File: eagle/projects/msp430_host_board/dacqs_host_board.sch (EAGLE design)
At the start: 68 parts, among them J1 MOL-KK-4P-V, J10 MOL-KK-3P-V, J11 CLM-112-02-L-D, J13 MOL-KK-2-V, J2 MOL-KK-4P-V, J3 MOL-KK-4P-V, J4 MOL-KK-4P-V, J5 MOL-KK-5P-V, J6 MOL-KK-3P-V, J7 MOL-KK-5P-V, J8 MOL-KK-3P-RA, J9 MOL-KK-3P-V, U1 Value, U2 Value, U3 PCT2075D,118, U4 MS560702BA03-50, U5 TPS61240DRVR, U6 LP5907_DBV_5, Y1 32.768kHz, Y2 4MHz, Y3 32.768kHz, Y4 4MHz

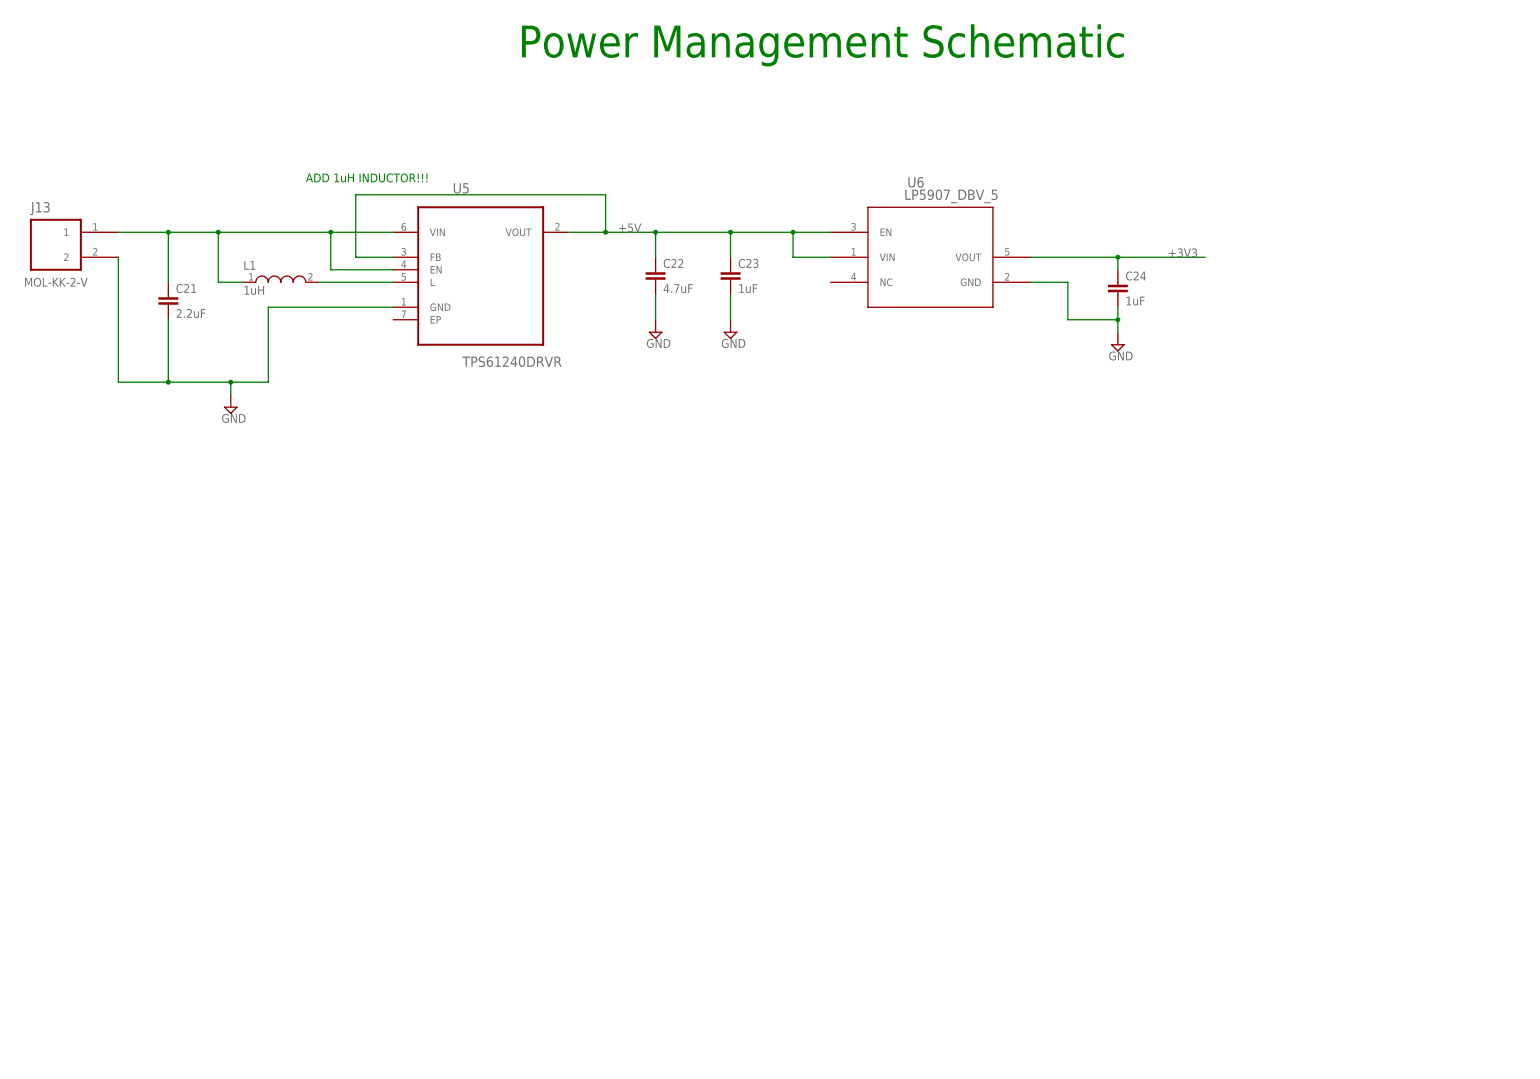
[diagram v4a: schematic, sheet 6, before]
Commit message: Added charging, current sense and motor battery voltage sensing
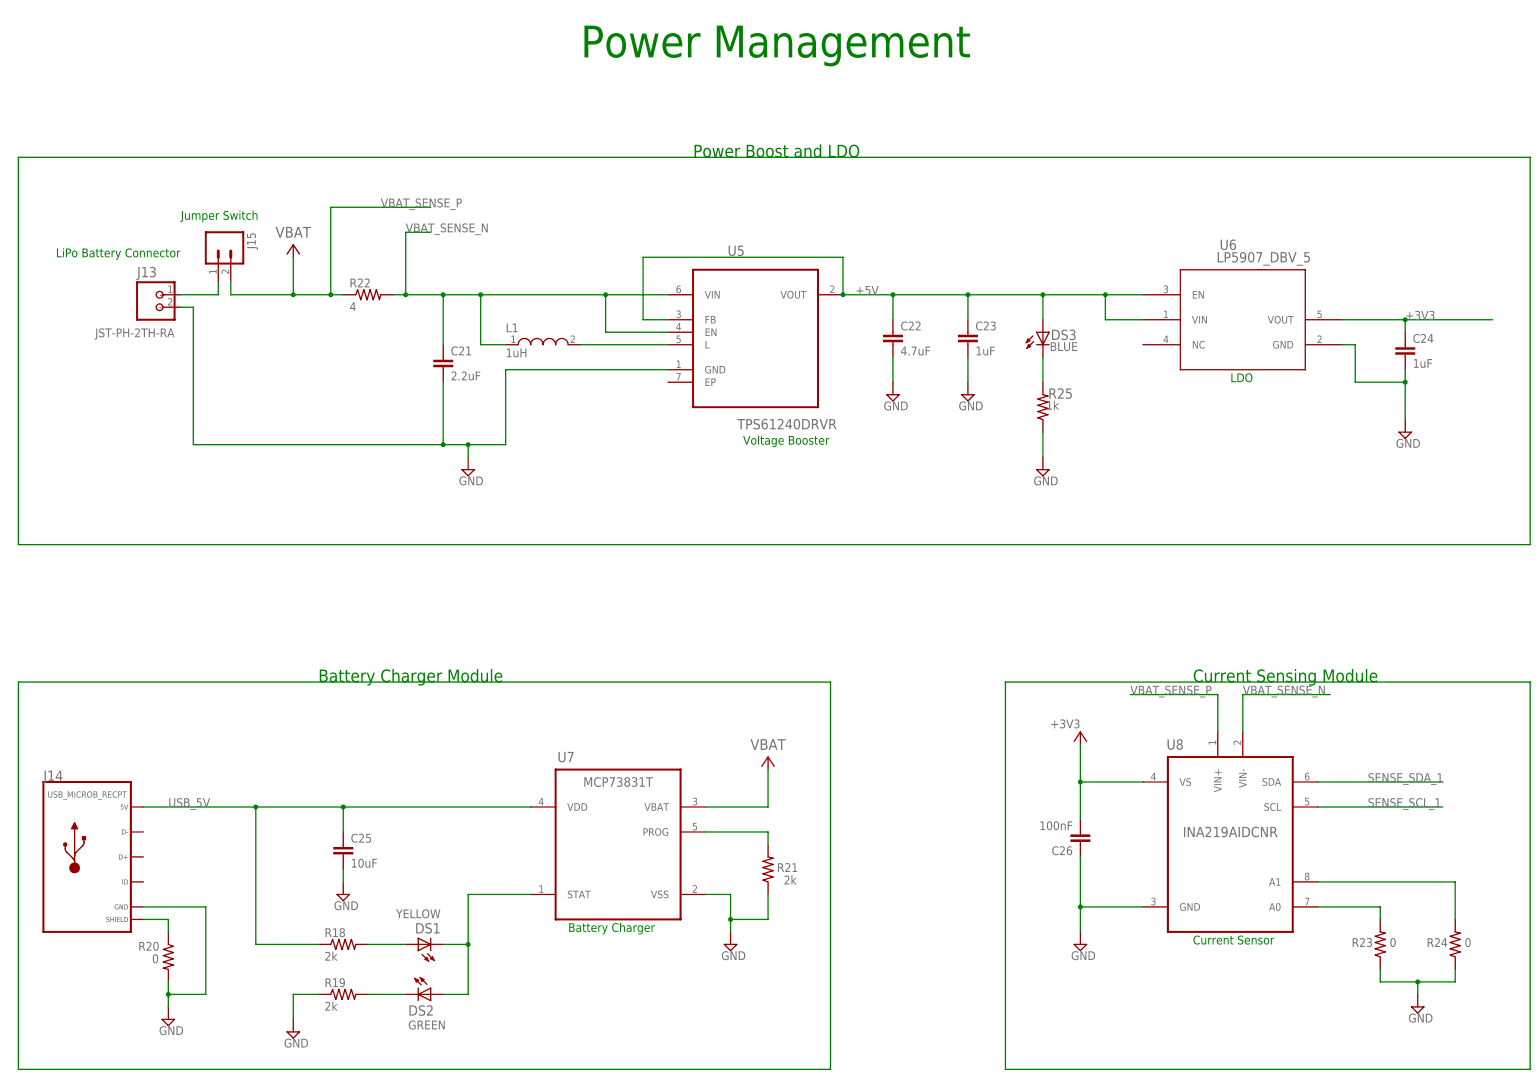
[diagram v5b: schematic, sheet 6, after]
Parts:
- added BAT1: (no value), daqcs_host:BC9VPC
- added C25: 10uF, daqcs_host:CAP_10UF0_0603
- added C26: 100nF, daqcs_host:CAP_100NF0_0603
- added DS1: YELLOW, daqcs_host:LED_Y2V0WURTH_0603
- added DS2: GREEN, daqcs_host:LED_G3V2WURTH_0603
- added DS3: BLUE, daqcs_host:LED_B3V2WURTH_0603
- added J14: USB_MICROB_RECPT, daqcs_host:USB_B_MICRO_RIGHT
- added J15: (no value), daqcs_host:M02PTH
- added J16: MOL-KK-2-RA, daqcs_host:MOLKK_2PIN_2RA_2RA
- added J18: MOL-KK-2-V, daqcs_host:MOLKK_2PIN2V_2V
- added R18, R19, R21: 2k, daqcs_host:RES_2R0_0603
- added R20, R23, R24: 0, daqcs_host:RES_0R0_0603
- added R22: 4, daqcs_host:RES_4R0_0603
- added R25: 1k, daqcs:RES_1R0_0603
- added R28: 10k, daqcs_host:RES_10R0_0603
- added R29: 27k, daqcs_host:RES_27R0_0603
- added U7: MCP73831T, daqcs_host:MCP73831T-2ATI/OT
- added U8: INA219AIDCNR, daqcs_host:INA219AIDCNR
- added U9: STD12NF06LT4, daqcs_host:STD12NF06LT4
- J13: value MOL-KK-2-V -> JST-PH-2TH-RA; device daqcs_host:MOLKK_2PIN2V_2V -> daqcs_host:JST-PH-2TH-RA_2TH-RA
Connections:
- new net 4V2_BAT: J18.1, R28.1
- new net CUTDOWN_EN: U1.P4.0_A8, U9.1
- new net MOTOR_BAT_VSENSE_1: R28.2, R29.2, U1.P3.0_A12_C12
- new net N$38: J14.SLD, R20.1
- new net N$39: J16.1
- new net N$40: BAT1.V+, J16.2
- new net N$41: DS2.C, R19.2
- new net N$42: DS1.C, DS2.A, U7.STAT
- new net N$43: DS1.A, R18.2
- new net N$44: R21.2, U7.PROG
- new net N$45: R23.2, U8.A0
- new net N$46: R24.2, U8.A1
- new net N$47: DS3.C, R25.2
- new net USB_5V: C25.1, J14.5V, R18.1, U7.VDD
- new net VBAT: U7.VBAT
- new net VBAT_SENSE_N: C21.1, L1.1, R22.2, U5.EN, U5.VIN, U8.VIN-
- new net VBAT_SENSE_P: J15.2, R22.1, U8.VIN+
- net +3V3: now also C26.2, U8.VS
- net +5V: now also DS3.A
- net GND: now also C25.2, C26.1, J14.GND, J18.2, R19.1, R20.2, R21.1, R23.1, R24.1, R25.1, R29.1, U7.VSS, U8.GND
- net N$36: now also J15.1; no longer C21.1, L1.1, U5.EN, U5.VIN
- net SENSE_SCL_1: now also U8.SCL
- net SENSE_SDA_1: now also U8.SDA
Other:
- note added: "Battery Charger"
- note added: "Battery Charger Module"
- note added: "Current Sensing Module"
- note added: "Current Sensor"
- note added: "Cutdown Switch and Connector"
- note added: "Host MSP430 Connectors"
- note added: "Jumper Switch"
- note added: "LDO"
- note added: "LiPo Battery Connector"
- note added: "Motor Battery Voltage Sense"
- note added: "Motor MSP430 Connectors"
- note added: "Power Boost and LDO"
- note added: "Power Management"
- note added: "Sensors and SD Card"
- note added: "Voltage Booster"
- note removed: "ADD 1uH INDUCTOR!!!"
- note removed: "Power Management Schematic"
- moved on the sheet: C21, C22, C23, C24, J10, J6, J7, J8, J9, L1, U5, U6

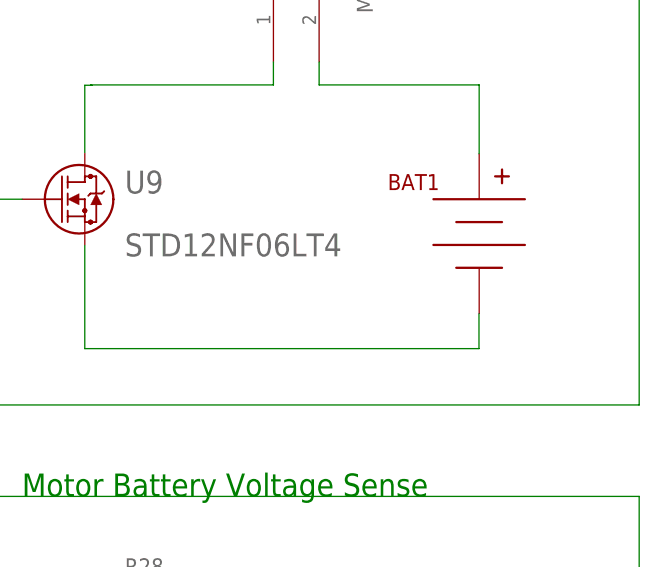
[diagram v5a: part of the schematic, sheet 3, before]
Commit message: Added 9V value to 9V battery connector
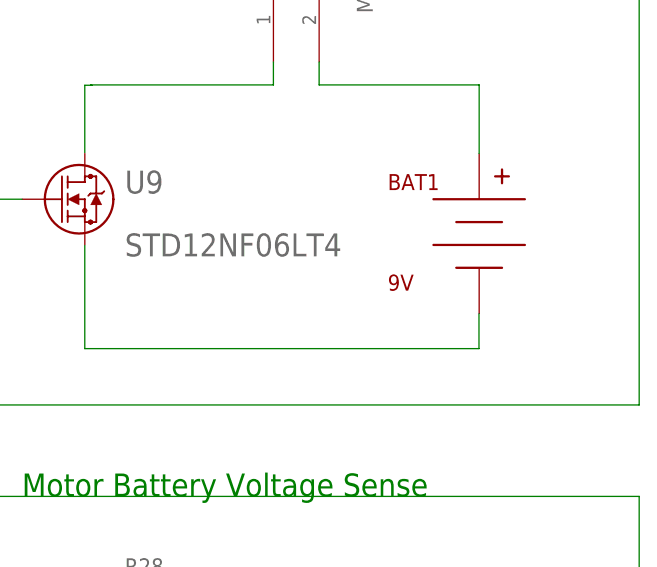
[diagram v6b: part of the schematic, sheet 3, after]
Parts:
- BAT1: value (none) -> 9V
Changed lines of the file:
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@@
 <setting verticaltext="up"/>
 </settings>
-<grid distance="0.1" unitdist="inch" unit="inch" style="lines" multiple="1" display="yes" altdistance="0.01" altunitdist="inch" altunit="inch"/>
+<grid distance="0.1" unitdist="inch" unit="inch" style="lines" multiple="1" display="no" altdistance="0.01" altunitdist="inch" altunit="inch"/>
 <layers>
 <layer number="1" name="Top" color="4" fill="1" visible="no" active="no"/>
@@
 <part name="J15" library="daqcs_host" deviceset="M02" device="PTH"/>
 <part name="U9" library="daqcs_host" deviceset="STD12NF06LT4" device=""/>
-<part name="BAT1" library="daqcs_host" deviceset="BC9VPC" device=""/>
+<part name="BAT1" library="daqcs_host" deviceset="BC9VPC" device="" value="9V"/>
 <part name="J16" library="daqcs_host" deviceset="MOLKK_2PIN" device="_2RA" technology="_2RA" value="MOL-KK-2-RA"/>
 <part name="J18" library="daqcs_host" deviceset="MOLKK_2PIN" device="_2V" technology="2V" value="MOL-KK-2-V"/>

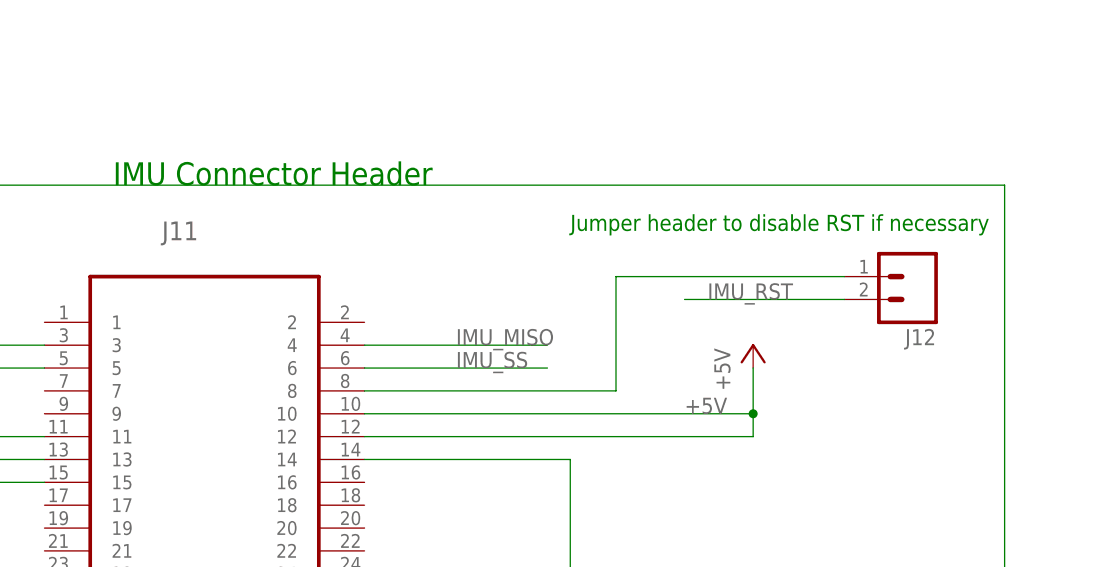
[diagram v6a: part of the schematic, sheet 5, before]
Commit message: Updates to library parts and schematic
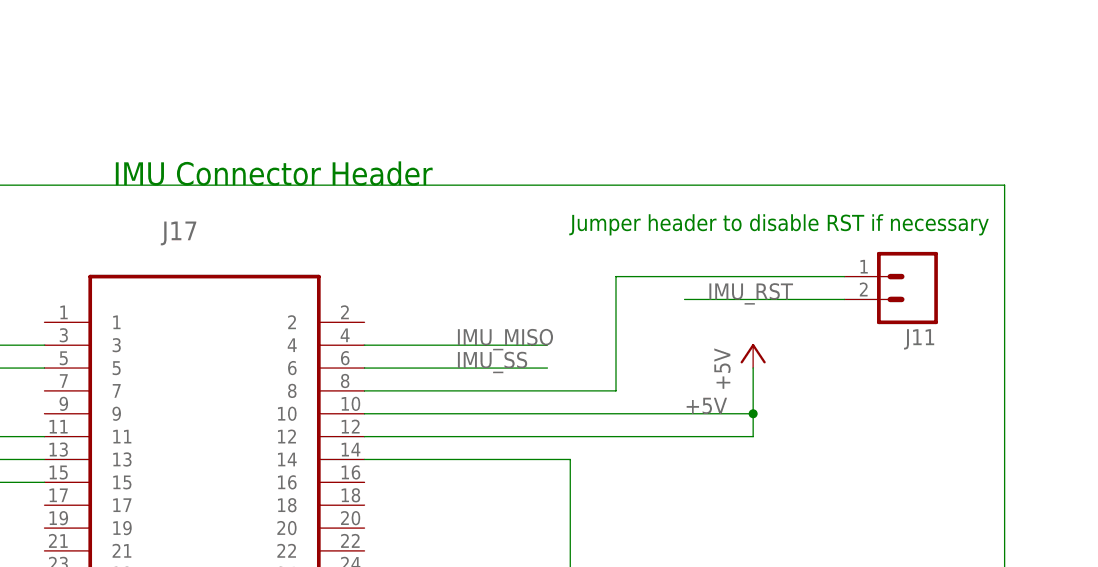
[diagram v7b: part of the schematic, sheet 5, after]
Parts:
- removed J12: (no value), SparkFun-Connectors:M02PTH
- added J17: CLM-112-02-L-D, daqcs_host:CLM-112-02-L-D
- J11: value CLM-112-02-L-D -> (none); device SAMTEC-BCS-CES-CLx_By_element14_Batch_1:CLM-112-02-L-D -> daqcs_host:M02PTH
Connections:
- net +5V: now also J17.10, J17.11, J17.12; no longer J11.10, J11.11, J11.12
- net GND: now also J17.13, J17.14, J17.15; no longer J11.13, J11.14, J11.15
- net IMU_MISO: now also J17.4; no longer J11.4
- net IMU_MOSI: now also J17.5; no longer J11.5
- net IMU_RST: now also J11.2; no longer J12.2
- net IMU_SCLK: now also J17.3; no longer J11.3
- net IMU_SS: now also J17.6; no longer J11.6
- net N$32: now also J11.1, J17.8; no longer J11.8, J12.1
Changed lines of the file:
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@@
 <part name="SUPPLY14" library="supply2" deviceset="GND" device=""/>
 <part name="+3V10" library="supply1" deviceset="+3V3" device=""/>
-<part name="J11" library="SAMTEC-BCS-CES-CLx_By_element14_Batch_1" deviceset="CLM-112-02-L-D" device=""/>
 <part name="P+1" library="supply1" deviceset="+5V" device=""/>
 <part name="SUPPLY15" library="supply2" deviceset="GND" device=""/>
 <part name="SUPPLY16" library="supply2" deviceset="GND" device=""/>
 <part name="P+2" library="supply1" deviceset="+5V" device=""/>
-<part name="J12" library="SparkFun-Connectors" deviceset="M02" device="PTH"/>
 <part name="U$1" library="daqcs_host" deviceset="MICROSD" device=""/>
 <part name="R16" library="daqcs_host" deviceset="RES" device="_0603" technology="_47R0" value="47k"/>
@@
 <part name="R29" library="daqcs_host" deviceset="RES" device="_0603" technology="_27R0" value="27k"/>
 <part name="SUPPLY32" library="supply2" deviceset="GND" device=""/>
+<part name="J17" library="daqcs_host" deviceset="CLM-112-02-L-D" device=""/>
+<part name="J11" library="daqcs_host" deviceset="M02" device="PTH"/>
 </parts>
 <sheets>
@@
 <instance part="SUPPLY14" gate="GND" x="312.42" y="170.18"/>
 <instance part="+3V10" gate="G$1" x="215.9" y="208.28"/>
-<instance part="J11" gate="A" x="93.98" y="78.74"/>
 <instance part="P+1" gate="1" x="43.18" y="86.36"/>
 <instance part="SUPPLY15" gate="GND" x="43.18" y="58.42"/>
 <instance part="SUPPLY16" gate="GND" x="134.62" y="58.42"/>
 <instance part="P+2" gate="1" x="154.94" y="86.36"/>
-<instance part="J12" gate="G$1" x="172.72" y="93.98" rot="R180"/>
 <instance part="U$1" gate="G$1" x="297.18" y="73.66"/>
 <instance part="R16" gate="G$1" x="238.76" y="86.36"/>
@@
 <instance part="SUPPLY18" gate="GND" x="269.24" y="43.18"/>
 <instance part="SUPPLY19" gate="GND" x="271.78" y="99.06" rot="R180"/>
+<instance part="J17" gate="A" x="93.98" y="78.74"/>
+<instance part="J11" gate="G$1" x="172.72" y="93.98" rot="R180"/>
 </instances>
 <busses>
@@
 </segment>
 <segment>
-<pinref part="J11" gate="A" pin="13"/>
 <pinref part="SUPPLY15" gate="GND" pin="GND"/>
 <wire x1="76.2" y1="73.66" x2="43.18" y2="73.66" width="0.1524" layer="91"/>
 <wire x1="43.18" y1="73.66" x2="43.18" y2="71.12" width="0.1524" layer="91"/>
-<pinref part="J11" gate="A" pin="15"/>
 <wire x1="43.18" y1="71.12" x2="43.18" y2="60.96" width="0.1524" layer="91"/>
 <wire x1="76.2" y1="71.12" x2="43.18" y2="71.12" width="0.1524" layer="91"/>
 <junction x="43.18" y="71.12"/>
-</segment>
-<segment>
-<pinref part="J11" gate="A" pin="14"/>
+<pinref part="J17" gate="A" pin="13"/>
+<pinref part="J17" gate="A" pin="15"/>
+</segment>
+<segment>
 <pinref part="SUPPLY16" gate="GND" pin="GND"/>
 <wire x1="111.76" y1="73.66" x2="134.62" y2="73.66" width="0.1524" layer="91"/>
 <wire x1="134.62" y1="73.66" x2="134.62" y2="60.96" width="0.1524" layer="91"/>
+<pinref part="J17" gate="A" pin="14"/>
 </segment>
 <segment>
@@
 <net name="IMU_SCLK" class="0">
 <segment>
-<pinref part="J11" gate="A" pin="3"/>
 <wire x1="76.2" y1="86.36" x2="55.88" y2="86.36" width="0.1524" layer="91"/>
 <label x="55.88" y="86.36" size="1.778" layer="95"/>
+<pinref part="J17" gate="A" pin="3"/>
 </segment>
 </net>
 <net name="IMU_MOSI" class="0">
 <segment>
-<pinref part="J11" gate="A" pin="5"/>
 <wire x1="76.2" y1="83.82" x2="55.88" y2="83.82" width="0.1524" layer="91"/>
 <label x="55.88" y="83.82" size="1.778" layer="95"/>
+<pinref part="J17" gate="A" pin="5"/>
 </segment>
 </net>
 <net name="IMU_MISO" class="0">
 <segment>
-<pinref part="J11" gate="A" pin="4"/>
 <wire x1="111.76" y1="86.36" x2="132.08" y2="86.36" width="0.1524" layer="91"/>
 <label x="121.92" y="86.36" size="1.778" layer="95"/>
+<pinref part="J17" gate="A" pin="4"/>
 </segment>
 </net>
 <net name="IMU_SS" class="0">
 <segment>
-<pinref part="J11" gate="A" pin="6"/>
 <wire x1="111.76" y1="83.82" x2="132.08" y2="83.82" width="0.1524" layer="91"/>
 <label x="121.92" y="83.82" size="1.778" layer="95"/>
+<pinref part="J17" gate="A" pin="6"/>
 </segment>
 </net>
 <net name="+5V" class="0">
 <segment>
-<pinref part="J11" gate="A" pin="11"/>
 <pinref part="P+1" gate="1" pin="+5V"/>
 <wire x1="76.2" y1="76.2" x2="43.18" y2="76.2" width="0.1524" layer="91"/>
 <wire x1="43.18" y1="76.2" x2="43.18" y2="83.82" width="0.1524" layer="91"/>
 <label x="50.8" y="76.2" size="1.778" layer="95"/>
-</segment>
-<segment>
-<pinref part="J11" gate="A" pin="10"/>
+<pinref part="J17" gate="A" pin="11"/>
+</segment>
+<segment>
 <pinref part="P+2" gate="1" pin="+5V"/>
 <wire x1="111.76" y1="78.74" x2="154.94" y2="78.74" width="0.1524" layer="91"/>
 <wire x1="154.94" y1="78.74" x2="154.94" y2="83.82" width="0.1524" layer="91"/>
-<pinref part="J11" gate="A" pin="12"/>
 <wire x1="111.76" y1="76.2" x2="154.94" y2="76.2" width="0.1524" layer="91"/>
 <wire x1="154.94" y1="76.2" x2="154.94" y2="78.74" width="0.1524" layer="91"/>
 <junction x="154.94" y="78.74"/>
 <label x="147.32" y="78.74" size="1.778" layer="95"/>
+<pinref part="J17" gate="A" pin="10"/>
+<pinref part="J17" gate="A" pin="12"/>
 </segment>
 </net>
 <net name="N$32" class="0">
 <segment>
-<pinref part="J11" gate="A" pin="8"/>
 <wire x1="111.76" y1="81.28" x2="139.7" y2="81.28" width="0.1524" layer="91"/>
 <wire x1="139.7" y1="81.28" x2="139.7" y2="93.98" width="0.1524" layer="91"/>
-<pinref part="J12" gate="G$1" pin="1"/>
 <wire x1="139.7" y1="93.98" x2="165.1" y2="93.98" width="0.1524" layer="91"/>
+<pinref part="J17" gate="A" pin="8"/>
+<pinref part="J11" gate="G$1" pin="1"/>
 </segment>
 </net>
 <net name="IMU_RST" class="0">
 <segment>
-<pinref part="J12" gate="G$1" pin="2"/>
 <wire x1="165.1" y1="91.44" x2="147.32" y2="91.44" width="0.1524" layer="91"/>
 <label x="149.86" y="91.44" size="1.778" layer="95"/>
-</segment>
-</net>
+<pinref part="J11" gate="G$1" pin="2"/>
+</segment>
+</net>
